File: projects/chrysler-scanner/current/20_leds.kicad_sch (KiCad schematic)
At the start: 16 parts, among them Q17 AO3400, Q18 AO3400, Q19 AO3400, Q20 AO3400

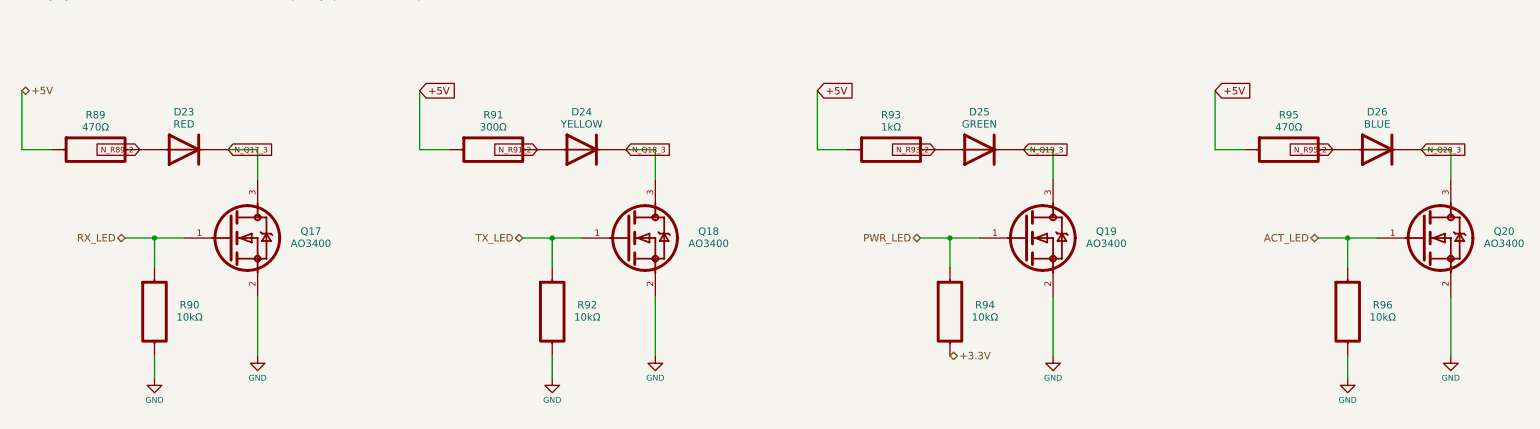
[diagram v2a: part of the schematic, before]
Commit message: Fix scanner protection, ADC isolation and health watchdog
Coordinate the bounded 12 V input clamp and programming FET/capacitor ratings, add powered-off ADC isolation, and supervise the AW9523B permit with a dedicated GPIO13 health heartbeat. Preserve original placements and document all deliberate source-PDF deviations.

Validation: native ERC and full DRC/parity/refill report zero findings; strict preservation/connectivity audit and final adversarial review pass within the documented prototype bounds. Regenerate Rev C PDF, BOM, manufacturing exports, processing sites and verified portable archives. Compatible firmware and bench/mechanical qualification remain required.
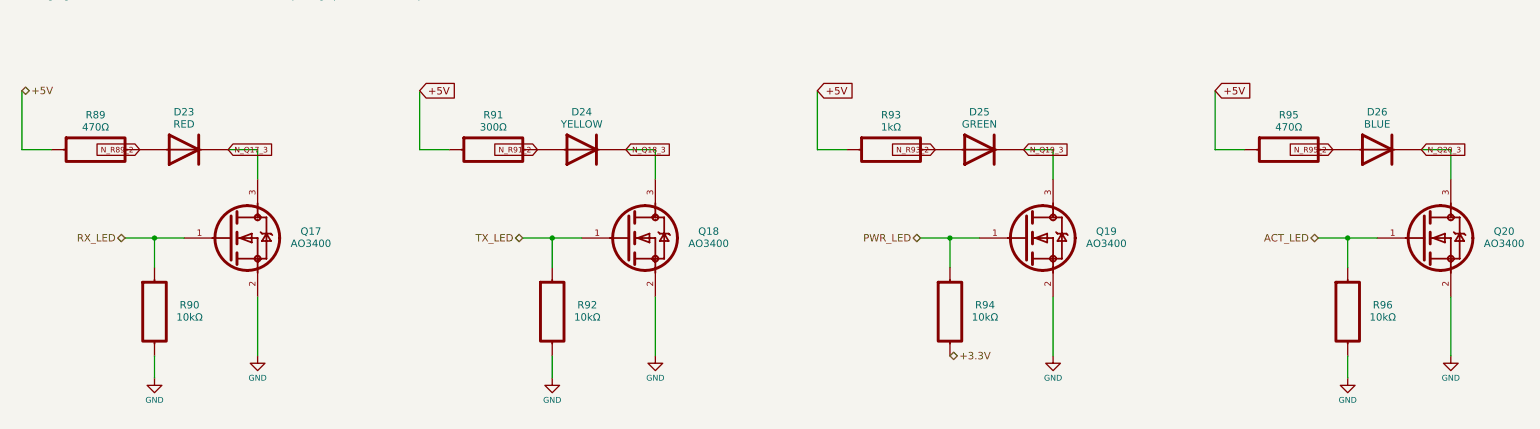
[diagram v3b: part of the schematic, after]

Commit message: Finish Chrysler scanner CCD correction and procurement fabrication package
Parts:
- D23: Assembly (none) -> PLACE; MPN (none) -> LTST-C150KRKT; Manufacturer (none) -> Lite-On; Procurement Source (none) -> https://optoelectronics.liteon.com/
- D24: Assembly (none) -> PLACE; MPN (none) -> LTST-C150KSKT; Manufacturer (none) -> Lite-On; Procurement Source (none) -> https://optoelectronics.liteon.com/
- D25: Assembly (none) -> PLACE; MPN (none) -> LTST-C150KGKT; Manufacturer (none) -> Lite-On; Procurement Source (none) -> https://optoelectronics.liteon.com/
- D26: Assembly (none) -> PLACE; MPN (none) -> LTST-C150TBKT; Manufacturer (none) -> Lite-On; Procurement Source (none) -> https://optoelectronics.liteon.com/
- Q17, Q18, Q19, Q20: Assembly (none) -> PLACE; MPN (none) -> AO3400A; Manufacturer (none) -> Alpha & Omega Semiconductor; Procurement Source (none) -> https://aosmd.com/sites/default/files/res/data_sheets/AO340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
- R89, R95: Assembly (none) -> PLACE; MPN (none) -> CRCW0603470RFKEA; Manufacturer (none) -> Vishay; Procurement Source (none) -> https://www.vishay.com/docs/20035/dcrcwe3.pdf; Selected Power Rating (none) -> 0.1W; Tolerance (none) -> 1%
- R90, R92, R94, R96: Assembly (none) -> PLACE; MPN (none) -> CRCW060310K0FKEA; Manufacturer (none) -> Vishay; Procurement Source (none) -> https://www.vishay.com/docs/20035/dcrcwe3.pdf; Selected Power Rating (none) -> 0.1W; Tolerance (none) -> 1%
- R91: Assembly (none) -> PLACE; MPN (none) -> CRCW0603300RFKEA; Manufacturer (none) -> Vishay; Procurement Source (none) -> https://www.vishay.com/docs/20035/dcrcwe3.pdf; Selected Power Rating (none) -> 0.1W; Tolerance (none) -> 1%
- R93: Assembly (none) -> PLACE; MPN (none) -> CRCW06031K00FKEA; Manufacturer (none) -> Vishay; Procurement Source (none) -> https://www.vishay.com/docs/20035/dcrcwe3.pdf; Selected Power Rating (none) -> 0.1W; Tolerance (none) -> 1%
